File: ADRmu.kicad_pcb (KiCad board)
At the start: 4 copper layers, 160 x 100 mm, 91 parts, among them J1 DIN41612_02x16_AC_EvenPins, J10 Conn_01x01, J11 Conn_01x01, J12 Conn_01x01, J2 10Vf, J3 10Vs, J4 ADR, J6 LoSense, J7 GND, J8 Conn_01x01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

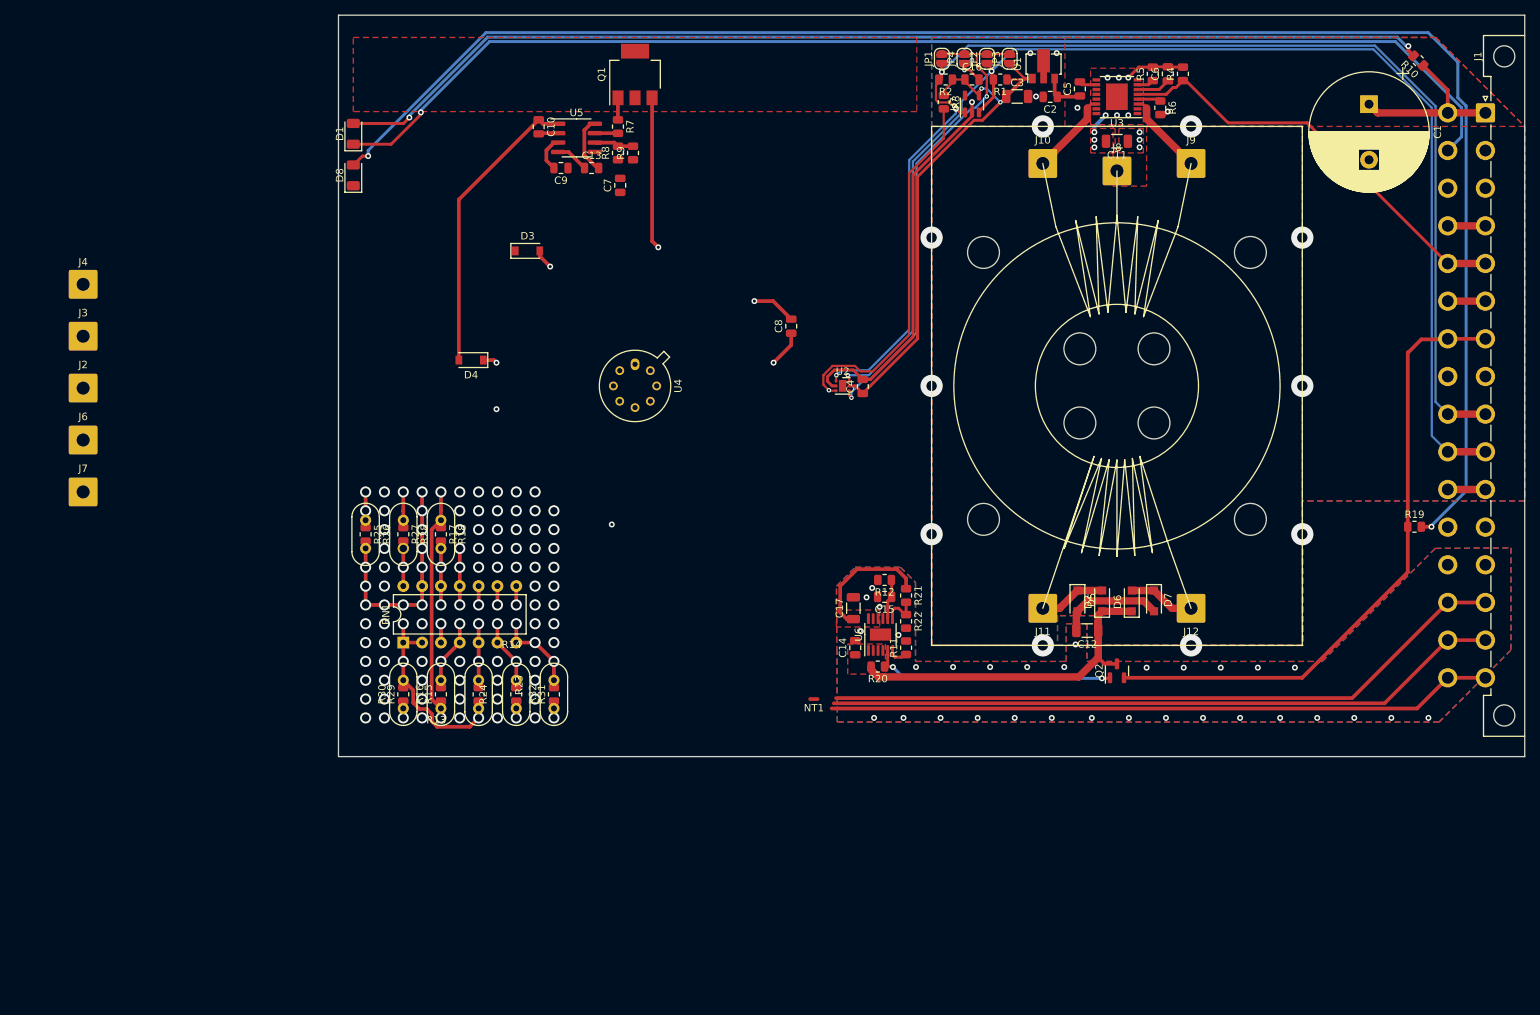
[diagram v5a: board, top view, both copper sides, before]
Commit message: added 10V buffer
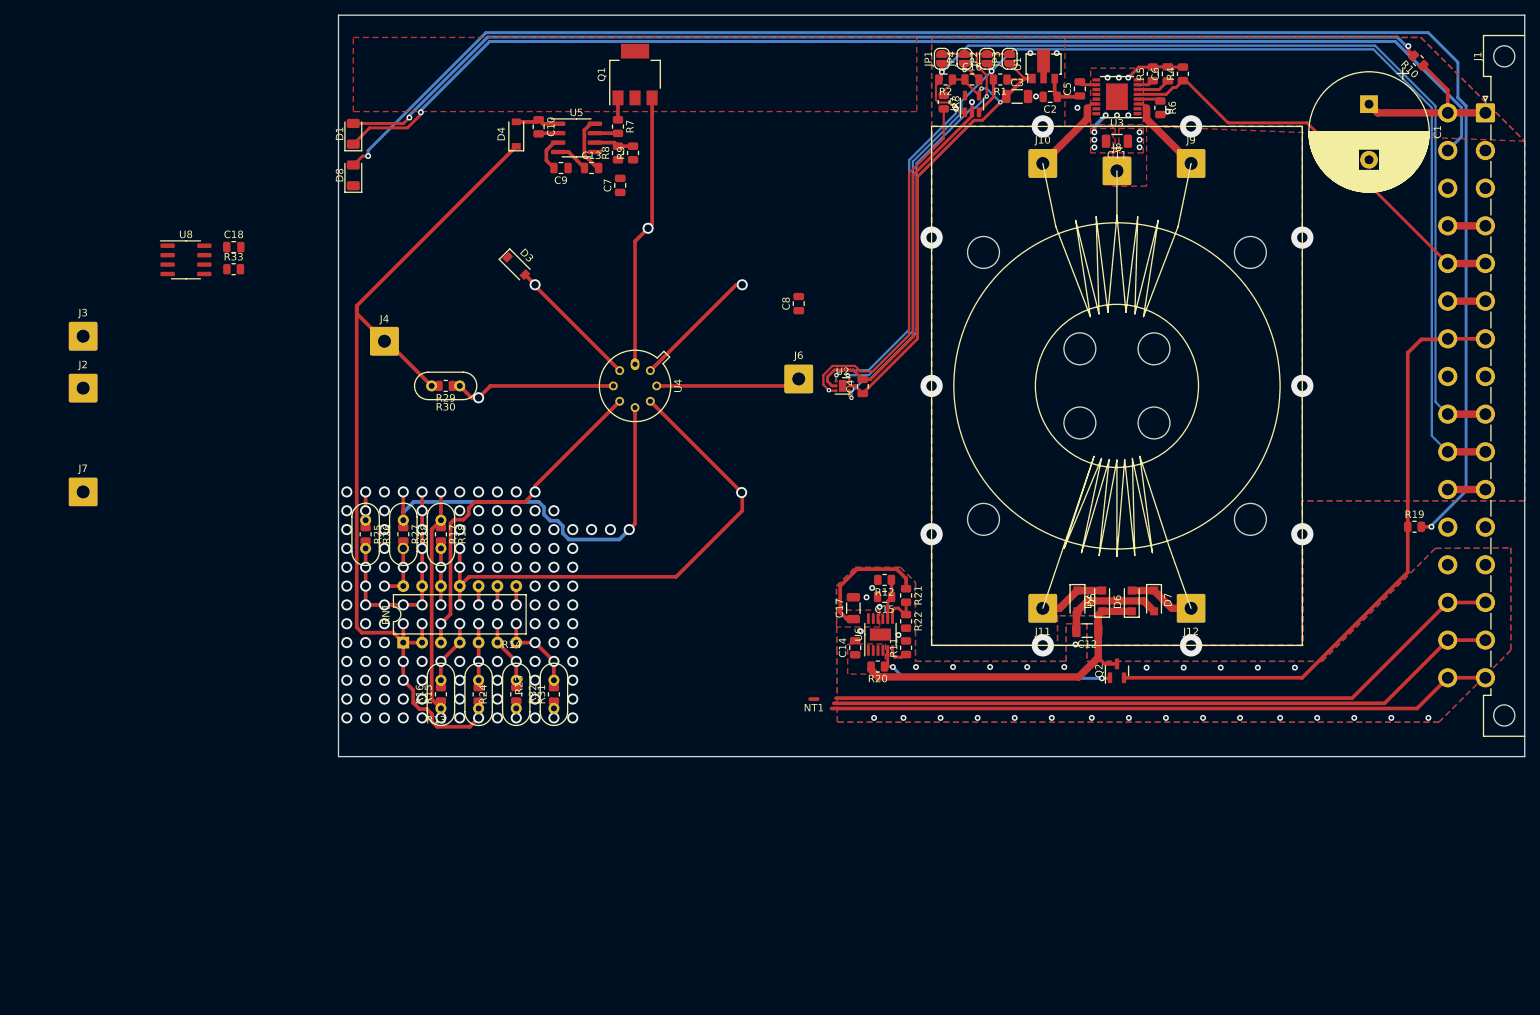
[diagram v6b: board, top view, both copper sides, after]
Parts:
- added C18: 100n, Capacitor_SMD:C_0805_2012Metric, F.Cu at (55.9, 81.3)
- added R33: 100R, Resistor_SMD:R_0805_2012Metric, F.Cu at (55.9, 84.3)
- added U8: ADA4523-1, Package_SO:SOIC-8_3.9x4.9mm_P1.27mm, F.Cu at (49.4, 83.0)
- moved J6 96.9 mm to (132.1, 99.1)
- moved R30 44.2 mm to (86.4, 100.0), turned to 180 degrees
- moved R29 42.0 mm to (84.5, 100.0), turned to 180 degrees
- moved J4 41.4 mm to (76.2, 94.0)
- moved D4 31.1 mm to (94.0, 66.0), turned to 90 degrees
- moved C8 3.21 mm to (132.1, 88.9)
- moved D3 2.54 mm to (94.0, 83.8), turned to -45 degrees
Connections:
- C12 pad 2: /DC-DC/0Vout -> /ref/ADR_Pin7
- C13 pad 1: /DC-DC/0Vout -> /ref/ADR_Pin7
- C14 pad 2: /DC-DC/0Vout -> /ref/ADR_Pin7
- C15 pad 2: /DC-DC/0Vout -> /ref/ADR_Pin7
- C17 pad 2: /DC-DC/0Vout -> /ref/ADR_Pin7
- D3 pad 1: /DC-DC/0Vout -> /ref/ADR_Pin7
- D5 pad 2: /DC-DC/0Vout -> /ref/ADR_Pin7
- D7 pad 2: /DC-DC/0Vout -> /ref/ADR_Pin7
- D8 pad 1: /DC-DC/0Vout -> /ref/ADR_Pin7
- J1 pad a26: /DC-DC/0Vout -> /ref/ADR_Pin7
- J1 pad c26: /DC-DC/0Vout -> /ref/ADR_Pin7
- J6 pad 1: /DC-DC/0Vout -> /ref/ADR_Pin7
- J7 pad 1: /DC-DC/0Vout -> /ref/ADR_Pin7
- NT1 pad 2: /DC-DC/0Vout -> /ref/ADR_Pin7
- R11 pad 2: /DC-DC/0Vout -> /ref/ADR_Pin7
- R12 pad 2: /DC-DC/0Vout -> /ref/ADR_Pin7
- R13 pad 2: Net-(R13-Pad2) -> /ref/10Vsense
- R14 pad 2: Net-(R13-Pad2) -> /ref/10Vsense
- R22 pad 2: /DC-DC/0Vout -> /ref/ADR_Pin7
- R31 pad 1: Net-(R31-Pad1) -> /ref/ADR_Pin7
- R32 pad 1: Net-(R31-Pad1) -> /ref/ADR_Pin7
- U5 pad 4: /DC-DC/0Vout -> /ref/ADR_Pin7
- U6 pad 13: /DC-DC/0Vout -> /ref/ADR_Pin7
- U6 pad 9: /DC-DC/0Vout -> /ref/ADR_Pin7
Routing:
- net /ref/ADR: track 62.3 -> 126.9 mm
- net Net-(C10-Pad1): track 39.7 -> 6.00 mm
- net /ref/ADR_Pin6: track 41.4 -> 69.8 mm, vias 3 -> 4
- net /ref/ADR_Pin8: track 44.5 -> 22.0 mm
- net /ref/ADR_Pin3: track 2.27 -> 23.0 mm
- net /ref/ADR_Pin5: track 41.8 -> 62.4 mm
- net /DC-DC/0Vout: track 18.7 -> 0.00 mm, vias 32 -> 0
- net Net-(D3-Pad2): track 36.5 -> 18.3 mm
- net Net-(C7-Pad1): track 52.7 -> 36.9 mm
- net /ref/ADR_Pin4: track 39.0 -> 49.9 mm, vias 1 -> 2
- net /ref/ADR_Pin7: track 69.6 -> 73.0 mm, vias 3 -> 35
- net Net-(R27-Pad2): track 6.07 -> 8.61 mm, vias 2 -> 3
- net Net-(R13-Pad2): track 2.27 -> 0.00 mm, vias 1 -> 0
- net /ref/10Vsense: track 91.4 -> 93.7 mm, vias 0 -> 1
- net Net-(R31-Pad1): track 2.26 -> 0.00 mm, vias 1 -> 0
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- added copper zone on B.Cu, net /ref/ADR_Pin7
- added copper zone on F.Cu, net /ref/ADR_Pin7
- added copper zone on In1.Cu, net /ref/ADR_Pin7
- added copper zone on In2.Cu, net /ref/ADR_Pin7
- removed copper zone on B.Cu, net /DC-DC/0Vout
- removed copper zone on F.Cu, net /DC-DC/0Vout
- removed copper zone on In1.Cu, net /DC-DC/0Vout
- removed copper zone on In2.Cu, net /DC-DC/0Vout

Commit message: the small reset
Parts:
- removed NT1: NetTie_2, NetTie:NetTie-2_SMD_Pad0.5mm
- removed R13, R23, R25, R27, R29, R31: dnp, Resistor_SMD:R_0805_2012Metric
- removed R14, R24, R26, R28, R30, R32: dnp, Crystal:Crystal_HC52-U_Vertical
- removed R15, R17: 0, Resistor_SMD:R_0805_2012Metric
- removed R16, R18: 0, Crystal:Crystal_HC52-U_Vertical
- added C19: 100n, Capacitor_SMD:C_0805_2012Metric, F.Cu at (56.9, 109.8)
- added NT2: NetTie_2, NetTie:NetTie-2_SMD_Pad0.5mm, F.Cu at (139.7, 109.2)
- J7: value GND -> GNDf
- moved C8 91.0 mm to (47.0, 121.4), turned to 0 degrees
- moved R9 82.6 mm to (48.8, 124.3), turned to 0 degrees
- moved C10 79.4 mm to (44.3, 124.5), turned to 0 degrees
- moved R8 69.1 mm to (57.2, 115.8), turned to 0 degrees
- moved C9 65.6 mm to (52.8, 116.2), turned to 0 degrees
- moved C7 64.8 mm to (56.9, 112.8), turned to 0 degrees
- moved J4 63.6 mm to (28.7, 136.3)
- moved RN1 57.0 mm to (27.1, 110.3), turned to 0 degrees
- moved J7 47.7 mm to (78.7, 134.6)
- moved J3 43.0 mm to (35.2, 136.3)
- moved J2 42.0 mm to (35.2, 142.3)
- moved U8 37.8 mm to (40.6, 119.7)
- moved R33 35.1 mm to (52.8, 119.2)
- moved D4 34.5 mm to (83.8, 99.1), turned to 180 degrees
- moved C18 29.0 mm to (61.3, 109.8)
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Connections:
- C12 pad 2: /ref/ADR_Pin7 -> /DC-DC/GNDf
- C13 pad 1: /ref/ADR_Pin7 -> /DC-DC/GNDf
- C13 pad 2: /DC-DC/12Vout -> /DC-DC/12Vf
- C14 pad 2: /ref/ADR_Pin7 -> /DC-DC/GNDf
- C15 pad 2: /ref/ADR_Pin7 -> /DC-DC/GNDf
- C17 pad 1: /DC-DC/12Vout -> /DC-DC/12Vf
- C17 pad 2: /ref/ADR_Pin7 -> /DC-DC/GNDf
- D3 pad 1: /ref/ADR_Pin7 -> /DC-DC/GNDf
- D4 pad 1: /ref/ADR -> /ref/ADR_Pin3
- D5 pad 2: /ref/ADR_Pin7 -> /DC-DC/GNDf
- D7 pad 2: /ref/ADR_Pin7 -> /DC-DC/GNDf
- D8 pad 1: /ref/ADR_Pin7 -> /DC-DC/GNDf
- J1 pad a26: /ref/ADR_Pin7 -> /DC-DC/GNDf
- J1 pad a28: Net-(J1-Pada28) -> /ref/ADR_Pin7
- J1 pad c26: /ref/ADR_Pin7 -> /DC-DC/GNDf
- J1 pad c28: Net-(J1-Pada28) -> /ref/ADR_Pin7
- J4 pad 1: /ref/ADR -> /ref/ADR_Pin3
- J7 pad 1: /ref/ADR_Pin7 -> /DC-DC/GNDf
- Q1 pad 2: /DC-DC/12Vout -> /DC-DC/12Vf
- R11 pad 2: /ref/ADR_Pin7 -> /DC-DC/GNDf
- R12 pad 2: /ref/ADR_Pin7 -> /DC-DC/GNDf
- R21 pad 1: /DC-DC/12Vout -> /DC-DC/12Vf
- R22 pad 2: /ref/ADR_Pin7 -> /DC-DC/GNDf
- RN1 pad 1: /ref/ADR -> /ref/ADR_Pin3
- RN1 pad 12: Net-(R17-Pad2) -> /ref/ADR_Pin7
- RN1 pad 13: Net-(R25-Pad2) -> /ref/ADR_Pin8
- RN1 pad 14: Net-(R27-Pad2) -> /ref/ADR_Pin5
- RN1 pad 2: /ref/ADR -> /ref/ADR_Pin3
- RN1 pad 4: Net-(R15-Pad2) -> /ref/ADR_Pin7
- RN1 pad 5: Net-(R23-Pad1) -> /ref/ADR_Pin3
- RN1 pad 6: Net-(R13-Pad1) -> /ref/10Vsense
- RN1 pad 7: Net-(R31-Pad2) -> /ref/ADR_Pin7
- U5 pad 4: /ref/ADR_Pin7 -> /DC-DC/GNDf
- U5 pad 8: /DC-DC/12Vout -> /DC-DC/12Vf
- U6 pad 10: /DC-DC/12Vout -> /DC-DC/12Vf
- U6 pad 11: /DC-DC/12Vout -> /DC-DC/12Vf
- U6 pad 12: /DC-DC/12Vout -> /DC-DC/12Vf
- U6 pad 13: /ref/ADR_Pin7 -> /DC-DC/GNDf
- U6 pad 9: /ref/ADR_Pin7 -> /DC-DC/GNDf
- U8 pad 3: /ref/ADR -> /ref/ADR_Pin3
- U8 pad 4: unconnected-(U8-Pad4) -> /DC-DC/GNDf
- U8 pad 7: unconnected-(U8-Pad7) -> /DC-DC/12Vf
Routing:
- net /DC-DC/GNDf: track 0.00 -> 201.5 mm, vias 0 -> 47
- net /ref/ADR: track 126.9 -> 0.00 mm, vias 5 -> 0
- net /DC-DC/12Vf: track 0.00 -> 104.0 mm
- net Net-(J1-Pada28): track 92.9 -> 0.00 mm
- net /ref/ADR_Pin7: track 73.0 -> 129.2 mm, vias 35 -> 1
- net /ref/ADR_Pin6: track 69.8 -> 19.9 mm, vias 4 -> 1
- net /ref/ADR_Pin5: track 62.4 -> 16.8 mm, vias 2 -> 1
- net Net-(R25-Pad2): track 31.5 -> 0.00 mm, vias 11 -> 0
- net /ref/ADR_Pin4: track 49.9 -> 19.0 mm, vias 2 -> 1
- net /DC-DC/12Vout: track 25.2 -> 0.00 mm
- net Net-(R31-Pad2): track 12.6 -> 0.00 mm, vias 3 -> 0
- net Net-(R15-Pad2): track 9.66 -> 0.00 mm, vias 2 -> 0
- net Net-(R13-Pad1): track 9.66 -> 0.00 mm, vias 2 -> 0
- net Net-(R23-Pad1): track 8.61 -> 0.00 mm, vias 2 -> 0
- net Net-(R27-Pad2): track 8.61 -> 0.00 mm, vias 3 -> 0
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- added copper zone on F.Cu, net /DC-DC/12Vf
- added copper zone on B.Cu, net /DC-DC/GNDf
- added copper zone on F.Cu, net /DC-DC/GNDf
- added copper zone on In1.Cu, net /DC-DC/GNDf
- added copper zone on In2.Cu, net /DC-DC/GNDf
- removed copper zone on F.Cu, net /DC-DC/12Vout
- removed copper zone on B.Cu, net /ref/ADR_Pin7
- removed copper zone on F.Cu, net /ref/ADR_Pin7
- removed copper zone on In1.Cu, net /ref/ADR_Pin7
- removed copper zone on In2.Cu, net /ref/ADR_Pin7

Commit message: ASDF!
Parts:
- moved J2 100.6 mm to (131.4, 113.0)
- moved J3 98.0 mm to (131.4, 118.1)
- moved U8 88.7 mm to (126.4, 142.2)
- moved C8 86.3 mm to (127.0, 88.9), turned to 135 degrees
- moved RN1 84.6 mm to (109.9, 128.3), turned to -90 degrees
- moved R33 83.5 mm to (132.4, 144.1)
- moved C13 78.3 mm to (85.7, 139.0), turned to 180 degrees
- moved C18 77.9 mm to (132.5, 141.6)
- moved C9 77.6 mm to (129.9, 107.3), turned to 180 degrees
- moved U5 75.8 mm to (79.9, 140.9)
- moved C19 75.1 mm to (126.5, 138.1)
- moved J4 66.2 mm to (87.6, 106.0)
- moved J7 60.7 mm to (137.2, 118.1)
- moved C7 44.6 mm to (90.2, 142.5), turned to -90 degrees
- moved R9 40.6 mm to (85.1, 142.5), turned to 90 degrees
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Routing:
- net /ref/ADR_Pin7: track 129.2 -> 253.5 mm
- net Net-(C7-Pad1): track 36.5 -> 152.6 mm, vias 0 -> 2
- net Net-(R7-Pad2): track 7.04 -> 106.5 mm
- net /ref/ADR_Pin5: track 16.8 -> 88.1 mm
- net /DC-DC/GNDf: track 201.5 -> 141.5 mm, vias 47 -> 49
- net Net-(C10-Pad1): track 0.00 -> 47.2 mm
- net /ref/10Vforce: track 89.9 -> 127.5 mm
- net /ref/ADR_Pin4: track 19.0 -> 55.7 mm
- net /ref/ADR_Pin8: track 17.2 -> 49.5 mm, vias 1 -> 0
- net /ref/10Vsense: track 91.4 -> 116.2 mm
- net /ref/ADR_Pin6: track 19.9 -> 41.0 mm
- net /ref/ADR_Pin3: track 22.0 -> 41.1 mm, vias 1 -> 0
- net /DC-DC/12Vf: track 104.0 -> 114.9 mm, vias 0 -> 2
- net Net-(R8-Pad2): track 0.00 -> 5.26 mm
- net Net-(Q1-Pad1): track 7.04 -> 2.45 mm
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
